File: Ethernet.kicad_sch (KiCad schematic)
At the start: 34 parts, among them J4 7499010211A, U8 LAN8742A, U9 USBLC6-4SC6, Y1 Crystal_GND24

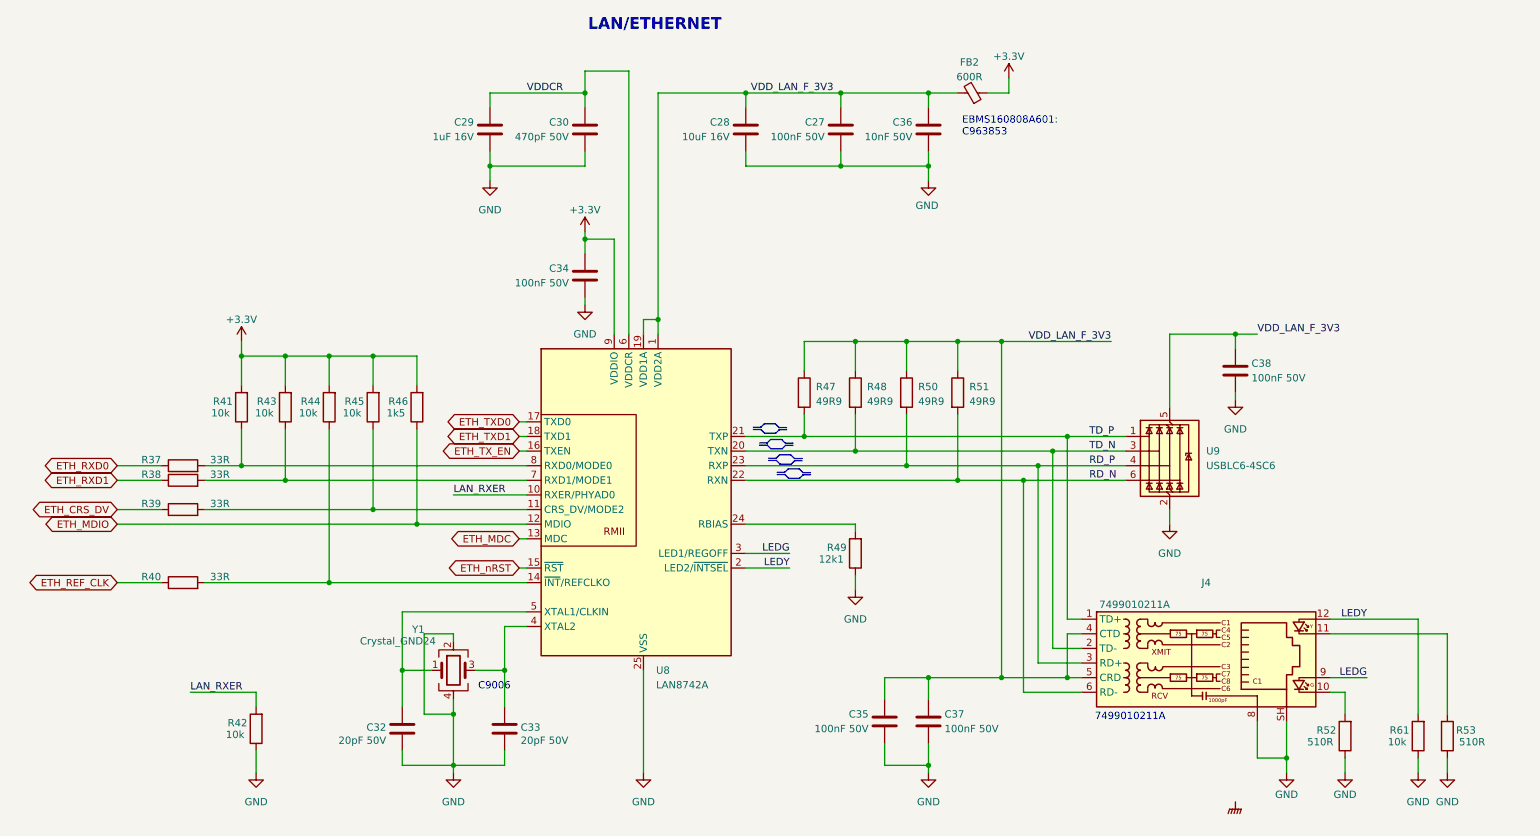
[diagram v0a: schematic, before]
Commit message: Se termina el circuito de entrada análoga, se escoge la bornera. Se termina las salidas de rele, se asumen que se trabajara maximo a 220V y solo para activar contactores. El circuito para el sensor namur se esta realizando
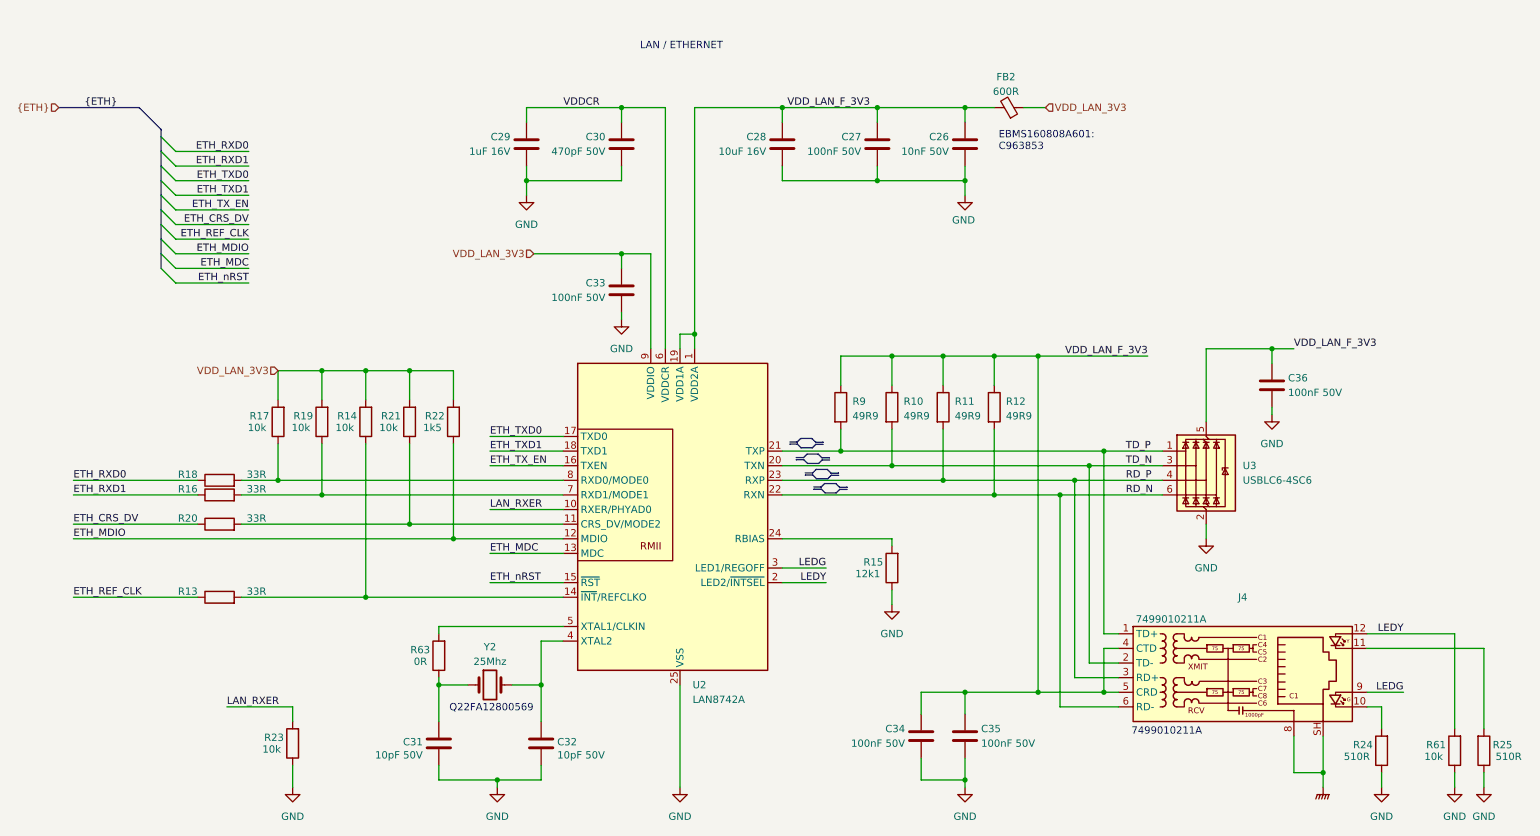
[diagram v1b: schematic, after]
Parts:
- removed C32: 20pF 50V, 1-Capacitor:C_0603_1608Metric, symbol 1-Capacitor:C_0805
- removed C36: 10nF 50V, 1-Capacitor:C_0603_1608Metric, symbol 1-Capacitor:C_0805
- removed R37, R38, R39, R40: 33R, 1-Resistor:R_0805_2012Metric, symbol Device:R
- removed R41, R42, R43, R44, R45: 10k, 1-Resistor:R_0805_2012Metric, symbol Device:R
- removed R46: 1k5, 1-Resistor:R_0805_2012Metric, symbol Device:R
- removed R47, R48, R50, R51: 49R9, 1-Resistor:R_0805_2012Metric, symbol Device:R
- removed R49: 12k1, 1-Resistor:R_0805_2012Metric, symbol Device:R
- removed R52, R53: 510R, 1-Resistor:R_0805_2012Metric, symbol Device:R
- removed U8: LAN8742A, Package_DFN_QFN:VQFN-24-1EP_4x4mm_P0.5mm_EP2.5x2.5mm_ThermalVias, symbol Interface_Ethernet:LAN8742A
- removed U9: USBLC6-4SC6, Package_TO_SOT_SMD:SOT-23-6, symbol Power_Protection:USBLC6-4SC6
- removed Y1: Crystal_GND24, 1-Crystal-and-Oscillator:Crystal_SMD_3225-4Pin_3.2x2.5mm, symbol 1-Crystal-and-Oscillator:Crystal_GND24
- added C26: 10nF 50V, symbol 1-Capacitor:C_0805
- added C31: 10pF 50V, symbol 1-Capacitor:C_0805
- added R10, R11, R12, R9: 49R9, symbol Device:R
- added R13, R16, R18, R20: 33R, symbol Device:R
- added R14, R17, R19, R21, R23: 10k, symbol Device:R
- added R15: 12k1, symbol Device:R
- added R22: 1k5, symbol Device:R
- added R24, R25: 510R, symbol Device:R
- added R63: 0R, symbol Device:R
- added U2: LAN8742A, Package_DFN_QFN:VQFN-24-1EP_4x4mm_P0.5mm_EP2.5x2.5mm_ThermalVias, symbol Interface_Ethernet:LAN8742A
- added U3: USBLC6-4SC6, Package_TO_SOT_SMD:SOT-23-6, symbol Power_Protection:USBLC6-4SC6
- added Y2: 25Mhz, symbol Device:Crystal
- C27, C28, C29, C30: footprint 1-Capacitor:C_0603_1608Metric -> (none)
- C32: renamed from C33; value 20pF 50V -> 10pF 50V; footprint 1-Capacitor:C_0603_1608Metric -> (none)
- C33: renamed from C34; footprint 1-Capacitor:C_0603_1608Metric -> (none)
- C34: renamed from C35; footprint 1-Capacitor:C_0805_2012Metric -> (none)
- C35: renamed from C37; footprint 1-Capacitor:C_0805_2012Metric -> (none)
- C36: renamed from C38; footprint 1-Capacitor:C_0805_2012Metric -> (none)
- J4: footprint 1-Connector:RJ45_Wuerth_7499010211A_Horizontal -> Connector_RJ:RJ45_Wuerth_7499010211A_Horizontal
- R61: footprint 1-Resistor:R_0805_2012Metric -> (none)
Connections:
- net ETH_CRS_DV: now also R20.1
- net ETH_MDC: now also U2.13 (MDC)
- net ETH_MDIO: now also R22.1, U2.12 (MDIO)
- net ETH_REF_CLK: now also R13.1
- net ETH_RXD0: now also R18.1
- net ETH_RXD1: now also R16.1
- net ETH_TXD0: now also U2.17 (TXD0)
- net ETH_TXD1: now also U2.18 (TXD1)
- net ETH_TX_EN: now also U2.16 (TXEN)
- net ETH_nRST: now also U2.15 (~{RST})
- net GND: now also C26.2, C31.2, R15.1, R23.1, R24.1, R25.1, U2.25 (VSS), U3.2 (GND); no longer J4.8, J4.SH
- net GNDPWR: now also J4.8, J4.SH
- net LAN_RXER: now also R23.2, U2.10 (RXER/PHYAD0)
- net LEDG: now also U2.3 (LED1/REGOFF)
- net LEDY: now also U2.2 (LED2/~{INTSEL})
- net RD_N: now also R12.2, U2.22 (RXN), U3.6 (I/O4)
- net RD_P: now also R11.2, U2.23 (RXP), U3.4 (I/O3)
- net TD_N: now also R10.2, U2.20 (TXN), U3.3 (I/O2)
- net TD_P: now also R9.2, U2.21 (TXP), U3.1 (I/O1)
- net VDDCR: now also U2.6 (VDDCR)
- net VDD_LAN_F_3V3: now also C26.1, R10.1, R11.1, R12.1, R9.1, U2.1 (VDD2A), U2.19 (VDD1A), U3.5 (VBUS)
- net at C32.1: now also U2.4 (XTAL2), Y2.2
- net at J4.10: now also R24.2
- net at J4.11: now also R25.2
- net +3.3V renamed VDD_LAN_3V3
- net VDD_LAN_3V3: now also R14.2, R17.2, R19.2, R21.2, R22.2, U2.9 (VDDIO)
- new net: R16.2, R19.1, U2.7 (RXD1/MODE1)
- new net: R13.2, R14.1, U2.14 (~{INT}/REFCLKO)
- new net: R15.2, U2.24 (RBIAS)
- new net: C31.1, R63.1, Y2.1
- new net: R63.2, U2.5 (XTAL1/CLKIN)
- new net: R17.1, R18.2, U2.8 (RXD0/MODE0)
- new net: R20.2, R21.1, U2.11 (CRS_DV/MODE2)
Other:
- note added: "LAN / ETHERNET"
- note added: "Q22FA12800569"
- note removed: "C9006"
- note removed: "LAN/ETHERNET"
- moved on the sheet: C27, C28, C29, C30, C32, C33, C34, C35, C36, FB2, J4, R61

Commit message: Avance
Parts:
- removed R63: 0R, symbol Device:R
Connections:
- net at C31.1, Y2.1: now also U2.5 (XTAL1/CLKIN)
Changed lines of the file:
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@@
 	(text "Q22FA12800569"
 		(exclude_from_sim no)
-		(at 104.394 136.144 0)
+		(at 104.394 136.652 0)
 		(effects
 			(font
@@
 	(wire
 		(pts
-			(xy 95.25 130.81) (xy 95.25 132.08)
+			(xy 95.25 121.92) (xy 95.25 132.08)
 		)
 		(stroke
@@
 	(wire
 		(pts
-			(xy 95.25 121.92) (xy 95.25 123.19)
-		)
-		(stroke
-			(width 0)
-			(type default)
-		)
-	)
-	(wire
-		(pts
 			(xy 173.99 107.95) (xy 173.99 106.68)
 		)
@@
 					(unit 1)
 				)
-			)
-		)
-	)
-	(symbol
-		(lib_id "Device:R")
-		(at 95.25 127 180)
-		(unit 1)
-		(exclude_from_sim no)
-		(in_bom yes)
-		(on_board yes)
-		(dnp no)
-		(property "Reference" "R63"
-			(at 93.726 125.984 0)
-			(effects
-				(font
-					(size 1.27 1.27)
-				)
-				(justify left)
-			)
-		)
-		(property "Value" "0R"
-			(at 93.218 128.016 0)
-			(effects
-				(font
-					(size 1.27 1.27)
-				)
-				(justify left)
-			)
-		)
-		(property "Footprint" ""
-			(at 97.028 127 90)
-			(effects
-				(font
-					(size 1.27 1.27)
-				)
-				(hide yes)
-			)
-		)
-		(property "Datasheet" "~"
-			(at 95.25 127 0)
-			(effects
-				(font
-					(size 1.27 1.27)
-				)
-				(hide yes)
-			)
-		)
-		(property "Description" "Resistor"
-			(at 95.25 127 0)
-			(effects
-				(font
-					(size 1.27 1.27)
-				)
-				(hide yes)
-			)
-		)
-		(pin "1"
-		)
-		(pin "2"
-		)
-		(instances
-			(project "Onyx_Client"
-				(path "/7cf65f8a-f9e1-4c97-ae3b-2bf5316c4d48/15cecee3-3ea4-4fda-9934-a7d023f81ee7"
-					(reference "R63")
-					(unit 1)
-				)
-			)
-			(project "Onyx_Client"
-				(path "/af529cf8-e3d6-4568-89be-bc7010f8b835/8e0b582f-0020-4bc2-aca5-707ed1850aed"
-					(reference "R63")
-					(unit 1)
-				)

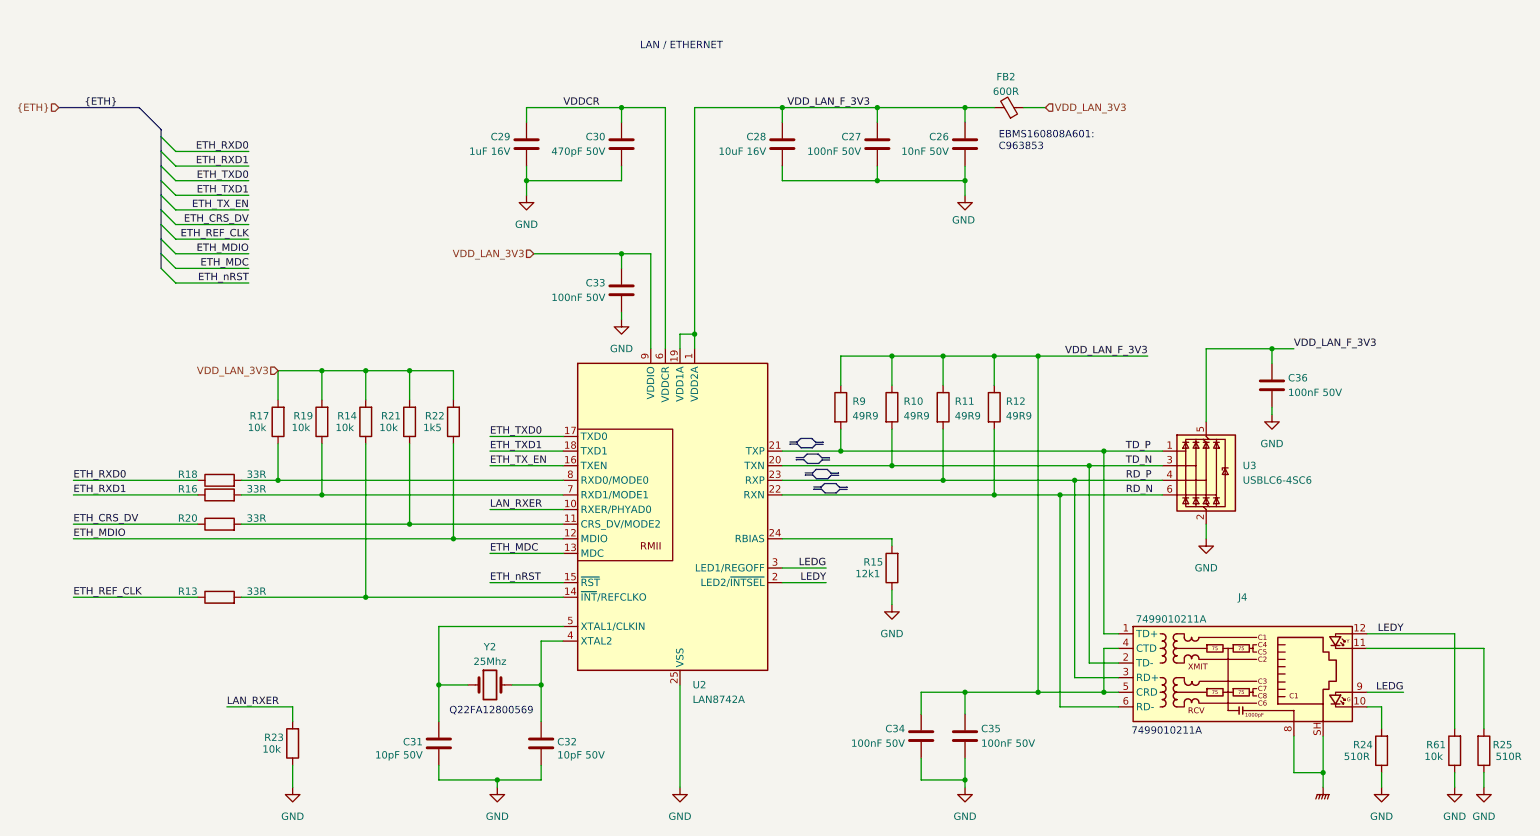
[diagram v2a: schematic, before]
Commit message: avance de pcb, se considera borneras externas para conexión de alimentación
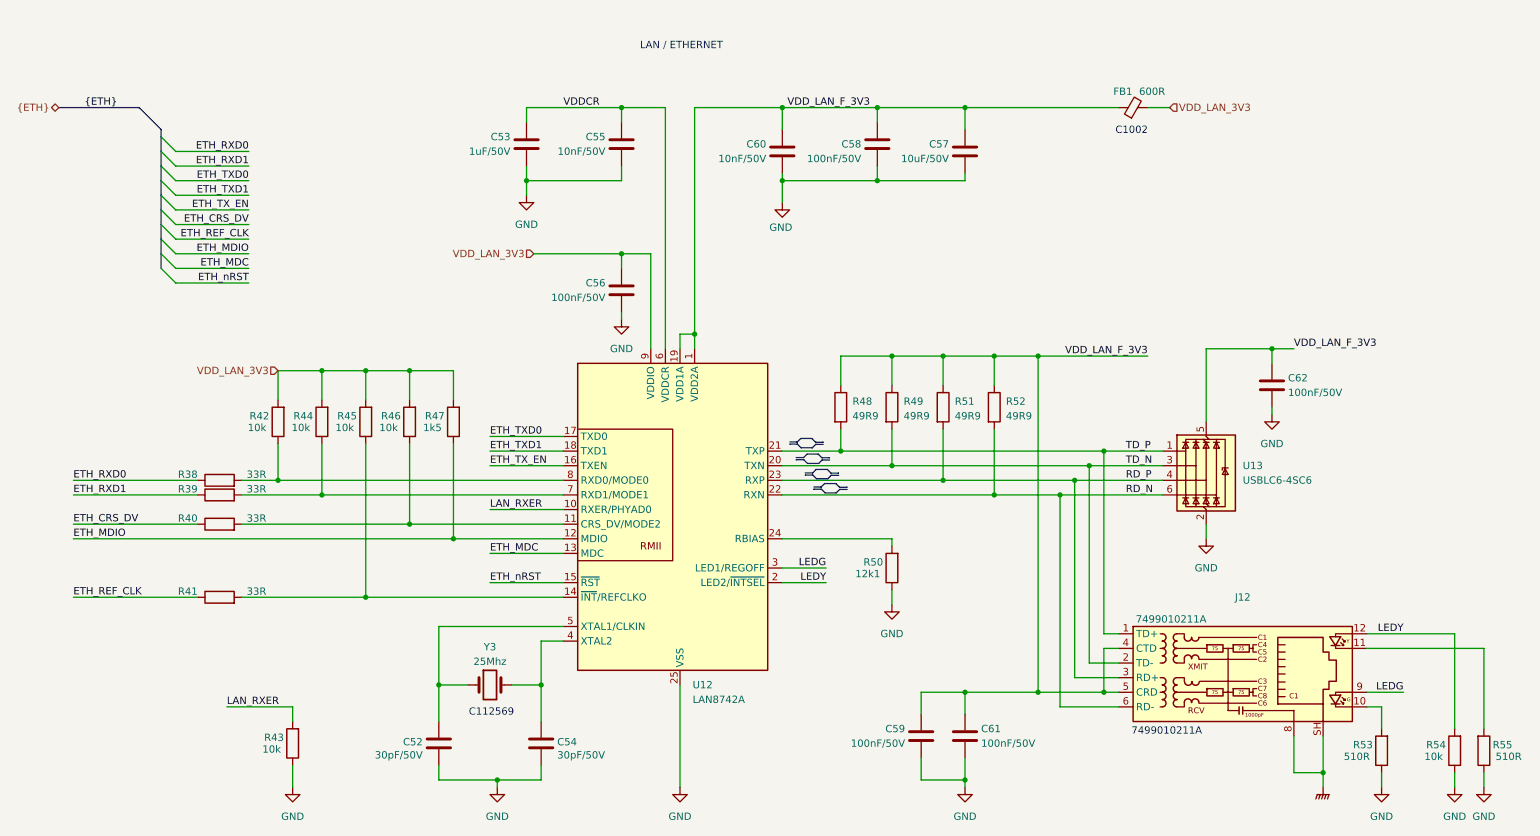
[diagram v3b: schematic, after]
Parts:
- removed C30: 470pF 50V, symbol 1-Capacitor:C_0805
- removed FB2: 600R, Inductor_SMD:L_0805_2012Metric, symbol Device:FerriteBead_Small
- added C55: 10nF/50V, Capacitor_SMD:C_0603_1608Metric, symbol 1-Capacitor:C_0805
- added FB1: 600R, Inductor_SMD:L_0805_2012Metric, symbol Device:FerriteBead_Small
- C52: renamed from C31; value 10pF 50V -> 30pF/50V; footprint (none) -> Capacitor_SMD:C_0603_1608Metric
- C53: renamed from C29; value 1uF 16V -> 1uF/50V; footprint (none) -> Capacitor_SMD:C_0805_2012Metric
- C54: renamed from C32; value 10pF 50V -> 30pF/50V; footprint (none) -> Capacitor_SMD:C_0603_1608Metric
- C56: renamed from C33; value 100nF 50V -> 100nF/50V; footprint (none) -> Capacitor_SMD:C_0603_1608Metric
- C57: renamed from C28; value 10uF 16V -> 10uF/50V; footprint (none) -> Capacitor_SMD:C_0603_1608Metric
- C58: renamed from C27; value 100nF 50V -> 100nF/50V; footprint (none) -> Capacitor_SMD:C_0603_1608Metric
- C59: renamed from C34; value 100nF 50V -> 100nF/50V; footprint (none) -> Capacitor_SMD:C_0603_1608Metric
- C60: renamed from C26; value 10nF 50V -> 10nF/50V; footprint (none) -> Capacitor_SMD:C_0603_1608Metric
- C61: renamed from C35; value 100nF 50V -> 100nF/50V; footprint (none) -> Capacitor_SMD:C_0603_1608Metric
- C62: renamed from C36; value 100nF 50V -> 100nF/50V; footprint (none) -> Capacitor_SMD:C_0603_1608Metric
- R38: renamed from R18; footprint (none) -> Resistor_SMD:R_0603_1608Metric
- R39: renamed from R16; footprint (none) -> Resistor_SMD:R_0603_1608Metric
- R40: renamed from R20; footprint (none) -> Resistor_SMD:R_0603_1608Metric
- R41: renamed from R13; footprint (none) -> Resistor_SMD:R_0603_1608Metric
- R42: renamed from R17; footprint (none) -> Resistor_SMD:R_0603_1608Metric
- R43: renamed from R23; footprint (none) -> Resistor_SMD:R_0603_1608Metric
- R44: renamed from R19; footprint (none) -> Resistor_SMD:R_0603_1608Metric
- R45: renamed from R14; footprint (none) -> Resistor_SMD:R_0603_1608Metric
- R46: renamed from R21; footprint (none) -> Resistor_SMD:R_0603_1608Metric
- R47: renamed from R22; footprint (none) -> Resistor_SMD:R_0603_1608Metric
- R48: renamed from R9; footprint (none) -> Resistor_SMD:R_0603_1608Metric
- R49: renamed from R10; footprint (none) -> Resistor_SMD:R_0603_1608Metric
- R50: renamed from R15; footprint (none) -> Resistor_SMD:R_0603_1608Metric
- R51: renamed from R11; footprint (none) -> Resistor_SMD:R_0603_1608Metric
- R52: renamed from R12; footprint (none) -> Resistor_SMD:R_0603_1608Metric
- R53: renamed from R24; footprint (none) -> Resistor_SMD:R_0603_1608Metric
- R54: renamed from R61; footprint (none) -> Resistor_SMD:R_0603_1608Metric
- R55: renamed from R25; footprint (none) -> Resistor_SMD:R_0603_1608Metric
- Y3: renamed from Y2; footprint (none) -> Crystal:Crystal_SMD_5032-2Pin_5.0x3.2mm
- renumbered J4 to J12, U2 to U12, U3 to U13
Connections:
- net GND: now also C55.2
- net VDDCR: now also C55.1
- net VDD_LAN_3V3: now also FB1.2
- net VDD_LAN_F_3V3: now also FB1.1
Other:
- note added: "C1002"
- note added: "C112569"
- note removed: "EBMS160808A601: C963853"
- note removed: "Q22FA12800569"
- moved on the sheet: C57, C60
